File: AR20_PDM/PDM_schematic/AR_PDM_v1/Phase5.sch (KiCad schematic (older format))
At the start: 15 parts, among them Q1 BTS50025-1TAD, U1 INA233

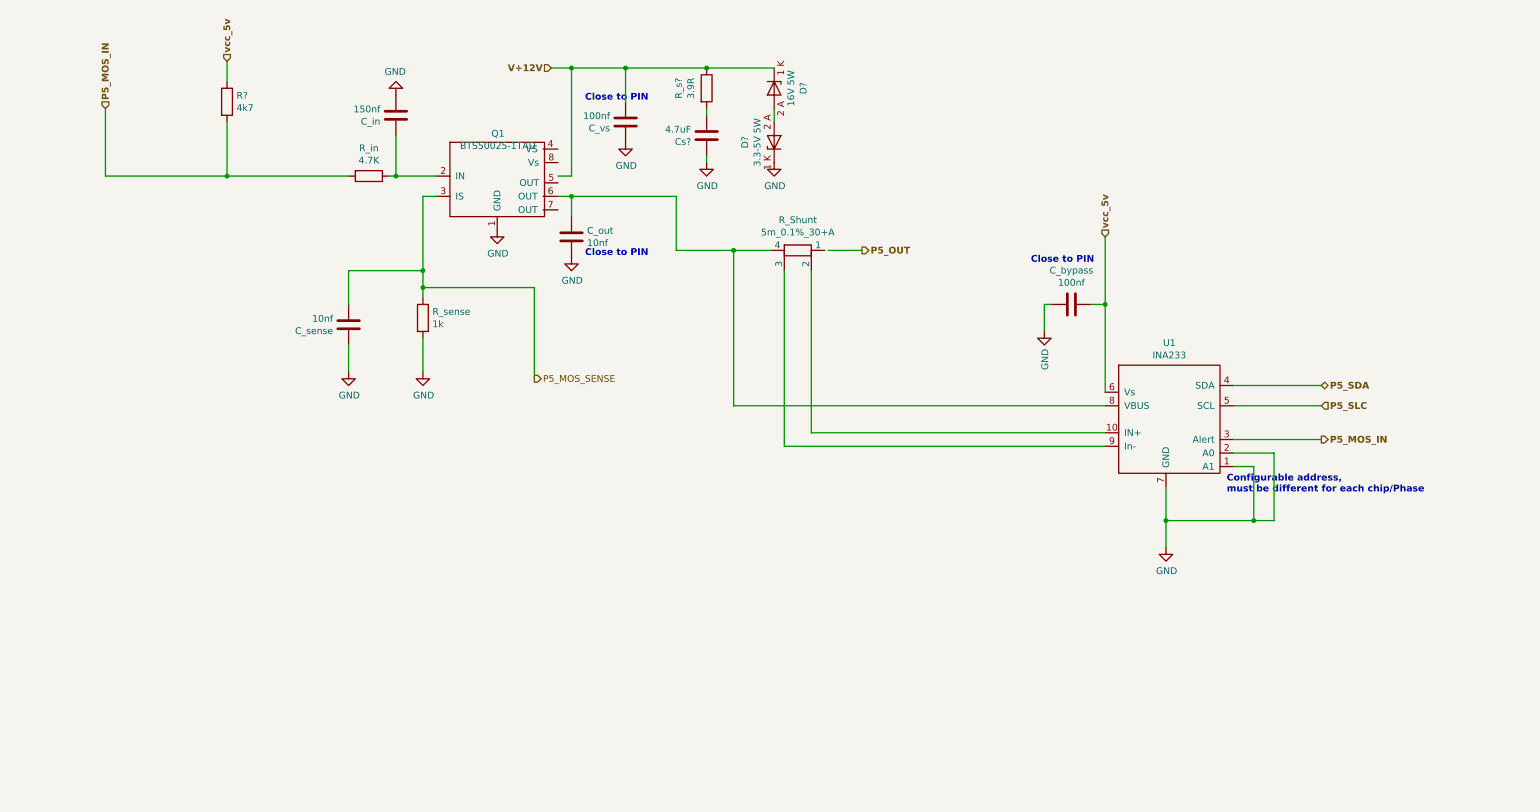
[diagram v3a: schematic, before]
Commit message: Fixed issues, controlled components, BOM, see discription
- added acm symbol
- fixed wrongly faced P-mosfets
- I/O expander now sinks led instead of source
- Bill of material mostly done
- Correct address for INA233 chips.
- Now 4 diodes serves as flyback for all mosfets
- Corrected naming scheme for compmonents (everything is not fixed yet)
- Fixed some labels
- altso some minor changes
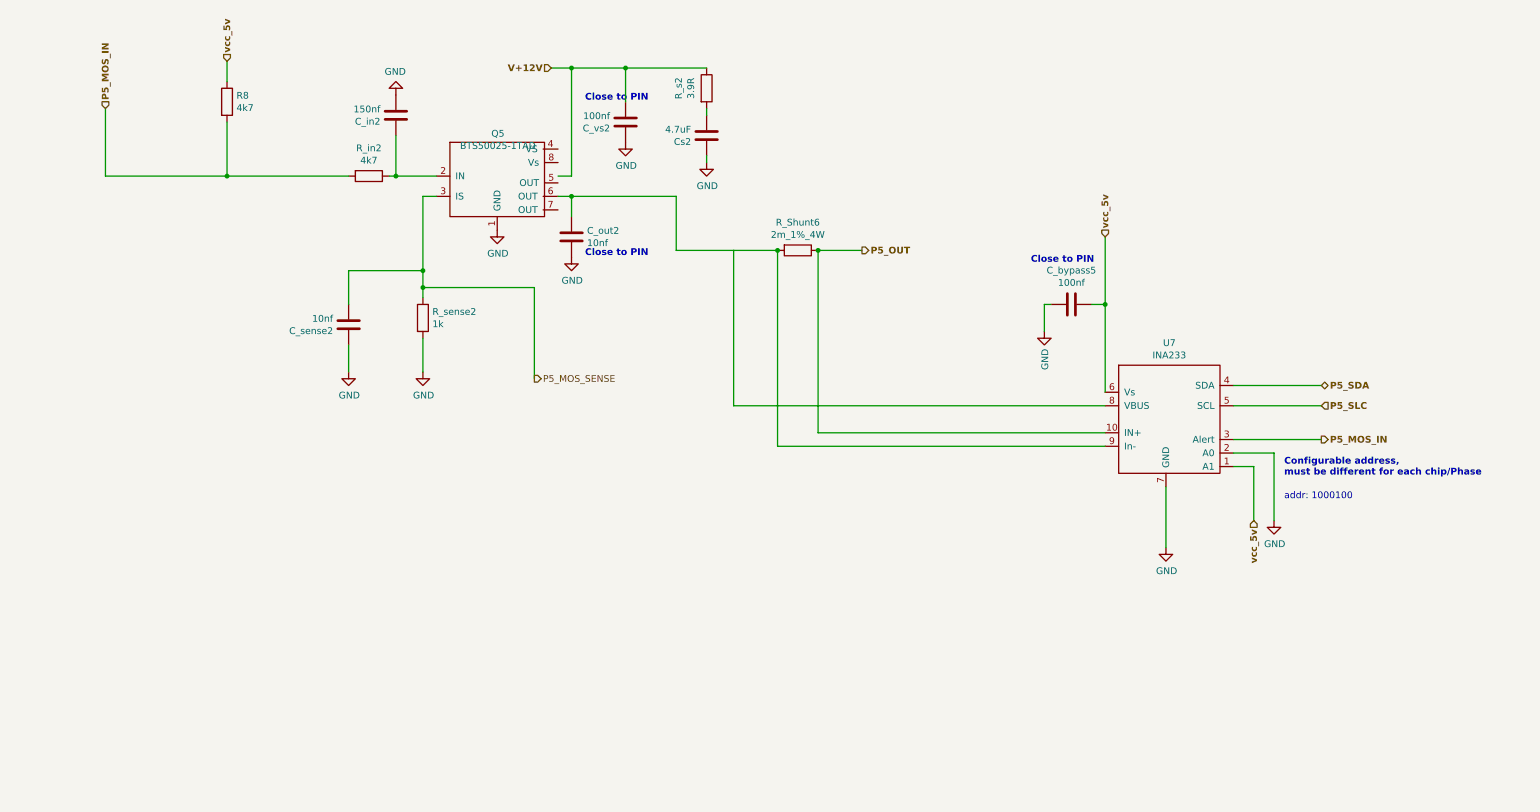
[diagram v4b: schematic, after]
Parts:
- removed C_bypass: 100nf, symbol AR20_PDM_v1-rescue:C-Device
- removed C_in: 150nf, symbol AR20_PDM_v1-rescue:C-Device
- removed C_out, C_sense: 10nf, symbol AR20_PDM_v1-rescue:C-Device
- removed Cs?: 4.7uF, symbol AR20_PDM_v1-rescue:C-Device
- removed D?: 3.3-5V 5W, symbol AR20_PDM_v1-rescue:D_Zener-Device
- removed D?: 16V 5W, symbol AR20_PDM_v1-rescue:D_Zener-Device
- removed Q1: BTS50025-1TAD, symbol AR20_PDM_v1-rescue:BTS50025-1TAD
- removed R?: 4k7, symbol AR20_PDM_v1-rescue:R-Device
- removed R_Shunt: 5m_0.1%_30+A, symbol AR20_PDM_v1-rescue:R_Shunt-Device
- removed R_in: 4.7K, symbol AR20_PDM_v1-rescue:R-Device
- removed R_s?: 3.9R, symbol AR20_PDM_v1-rescue:R-Device
- removed R_sense: 1k, symbol AR20_PDM_v1-rescue:R-Device
- removed U1: INA233, symbol AR20_PDM_v1-rescue:INA233
- added C_bypass5: 100nf, Capacitor_SMD:C_0603_1608Metric, symbol AR20_PDM_v1-rescue:C-Device
- added C_in2: 150nf, Capacitor_SMD:C_0603_1608Metric, symbol AR20_PDM_v1-rescue:C-Device
- added C_out2, C_sense2: 10nf, Capacitor_SMD:C_0603_1608Metric, symbol AR20_PDM_v1-rescue:C-Device
- added Cs2: 4.7uF, Capacitor_SMD:C_1206_3216Metric, symbol AR20_PDM_v1-rescue:C-Device
- added Q5: BTS50025-1TAD, symbol AR20_PDM_v1-rescue:BTS50025-1TAD
- added R8, R_in2: 4k7, symbol AR20_PDM_v1-rescue:R-Device
- added R_Shunt6: 2m_1%_4W, symbol AR20_PDM_v1-rescue:R-Device
- added R_s2: 3.9R, symbol AR20_PDM_v1-rescue:R-Device
- added R_sense2: 1k, symbol AR20_PDM_v1-rescue:R-Device
- added U7: INA233, symbol AR20_PDM_v1-rescue:INA233
- C_vs2: renamed from C_vs; footprint (none) -> Capacitor_SMD:C_0603_1608Metric
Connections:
- wire segments 57 -> 52
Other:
- note added: "addr: 1000100"

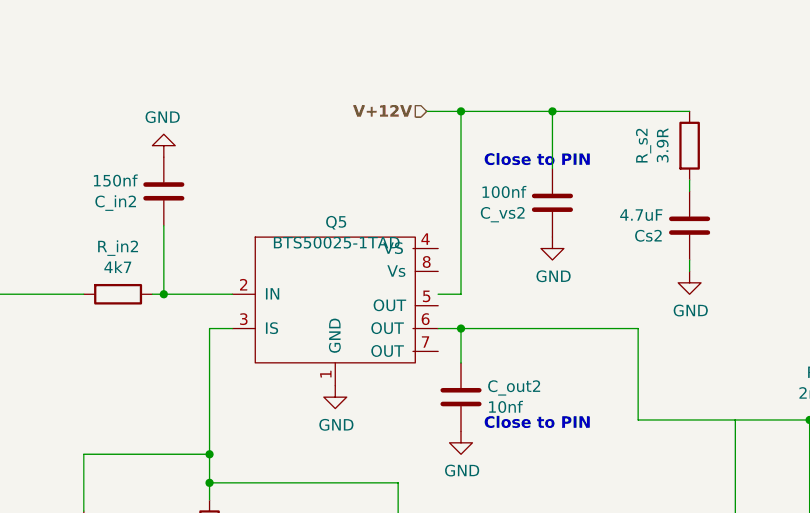
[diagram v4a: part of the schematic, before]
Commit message: PCB design, and issue fixing, work in progress
- Error fixed: Mux mosfet resistor change to ground
- Open drain output added on phase 6, for engine blipping purpose
- Most of pcb symbols and footprints are finished, including main connector
- PCB is change from 1oz to 2oz copper layer, for easier routing.
- Basic Draft of pcb is done, for now.
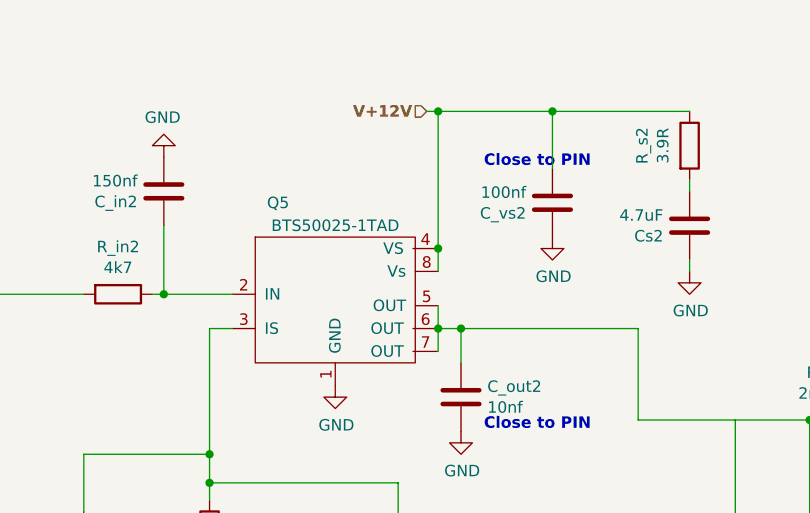
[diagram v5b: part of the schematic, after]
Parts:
- Q5: footprint (none) -> AR_PDM_v1:BTS500xx
- R8, R_in2, R_s2, R_sense2: footprint (none) -> Resistor_SMD:R_0603_1608Metric
- R_Shunt6: footprint (none) -> Resistor_SMD:R_2512_6332Metric
- U7: footprint (none) -> AR_PDM_v1:INA233
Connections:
- net V+12V: now also Q5.4 (VS), Q5.8 (Vs)
- net at C_out2.1, Q5.6 (OUT), R_Shunt6.2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: now also Q5.5 (OUT), Q5.7 (OUT)
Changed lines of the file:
@@
 F 0 "R_in2" V 3093 2400 50  0000 C CNN
 F 1 "4k7" V 3184 2400 50  0000 C CNN
-F 2 "" V 3230 2400 50  0001 C CNN
+F 2 "Resistor_SMD:R_0603_1608Metric" V 3230 2400 50  0001 C CNN
 F 3 "~" H 3300 2400 50  0001 C CNN
 	1    3300 2400
@@
 F 0 "R8" H 2320 1896 50  0000 L CNN
 F 1 "4k7" H 2320 1805 50  0000 L CNN
-F 2 "" V 2180 1850 50  0001 C CNN
+F 2 "Resistor_SMD:R_0603_1608Metric" V 2180 1850 50  0001 C CNN
 F 3 "~" H 2250 1850 50  0001 C CNN
 	1    2250 1850
@@
 AR Path="/5E0FDCCC/5E21B7FF" Ref="Q?"  Part="1"
 AR Path="/5E10174B/5E21B7FF" Ref="Q?"  Part="1"
-F 0 "Q5" H 4255 3215 50  0000 C CNN
-F 1 "BTS50025-1TAD" H 4255 3124 50  0000 C CNN
-F 2 "" H 4250 2650 50  0001 C CNN
+F 0 "Q5" H 4000 3300 50  0000 C CNN
+F 1 "BTS50025-1TAD" H 4250 3200 50  0000 C CNN
+F 2 "AR_PDM_v1:BTS500xx" H 4250 2650 50  0001 C CNN
 F 3 "" H 4250 2650 50  0001 C CNN
 	1    4250 2650
@@
 F 0 "U7" H 9225 4465 50  0000 C CNN
 F 1 "INA233" H 9225 4374 50  0000 C CNN
-F 2 "" H 9200 4050 50  0001 C CNN
+F 2 "AR_PDM_v1:INA233" H 9200 4050 50  0001 C CNN
 F 3 "" H 9200 4050 50  0001 C CNN
 	1    9200 4050
@@
 Wire Wire Line
 	3700 3100 3700 3225
-Wire Wire Line
-	4700 2400 4800 2400
-Wire Wire Line
-	4800 2400 4800 1600
-Wire Wire Line
-	4800 1600 4650 1600
 Text HLabel 2250 1550 1    50   Input ~ 10
 vcc_5v
@@
 F 0 "R_s2" V 5593 1750 50  0000 C CNN
 F 1 "3.9R" V 5684 1750 50  0000 C CNN
-F 2 "" V 5730 1750 50  0001 C CNN
+F 2 "Resistor_SMD:R_0603_1608Metric" V 5730 1750 50  0001 C CNN
 F 3 "~" H 5800 1750 50  0001 C CNN
 	1    5800 1750
@@
 Wire Wire Line
 	5200 1600 5800 1600
-Wire Wire Line
-	4800 1600 5200 1600
-Connection ~ 4800 1600
 Connection ~ 5200 1600
 Text HLabel 1350 1900 1    50   Input ~ 10
@@
 F 0 "R_sense2" H 3770 3496 50  0000 L CNN
 F 1 "1k" H 3770 3405 50  0000 L CNN
-F 2 "" V 3630 3450 50  0001 C CNN
+F 2 "Resistor_SMD:R_0603_1608Metric" V 3630 3450 50  0001 C CNN
 F 3 "~" H 3700 3450 50  0001 C CNN
 	1    3700 3450
@@
 F 0 "R_Shunt6" V 6268 2950 50  0000 C CNN
 F 1 "2m_1%_4W" V 6359 2950 50  0000 C CNN
-F 2 "" V 6405 2950 50  0001 C CNN
+F 2 "Resistor_SMD:R_2512_6332Metric" V 6405 2950 50  0001 C CNN
 F 3 "~" H 6475 2950 50  0001 C CNN
 	1    6475 2950
@@
 Text HLabel 9850 4950 3    50   Input ~ 10
 vcc_5v
+Wire Wire Line
+	4700 2550 4700 2650
+Connection ~ 4700 2550
+Wire Wire Line
+	4700 2550 4700 2450
+Wire Wire Line
+	4650 1600 4700 1600
+Wire Wire Line
+	4700 2300 4700 2200
+Wire Wire Line
+	4700 2200 4700 1600
+Connection ~ 4700 2200
+Connection ~ 4700 1600
+Wire Wire Line
+	4700 1600 5200 1600
 $EndSCHEMATC

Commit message: PCB Design, Work in progress
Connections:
- net P5_Shunt: now reaches C_out2.1, Q5.5 (OUT), Q5.6 (OUT), Q5.7 (OUT), R_Shunt6.2, U7.8 (VBUS), U7.9 (In-)
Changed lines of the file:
@@
 $Descr A4 11693 8268
 encoding utf-8
-Sheet 6 13
+Sheet 5 13
 Title ""
 Date ""
@@
 Wire Wire Line
 	4700 1600 5200 1600
+Wire Wire Line
+	6000 2950 6000 2825
+Text HLabel 6000 2825 1    50   Input ~ 0
+P5_Shunt
+Connection ~ 6000 2950
 $EndSCHEMATC

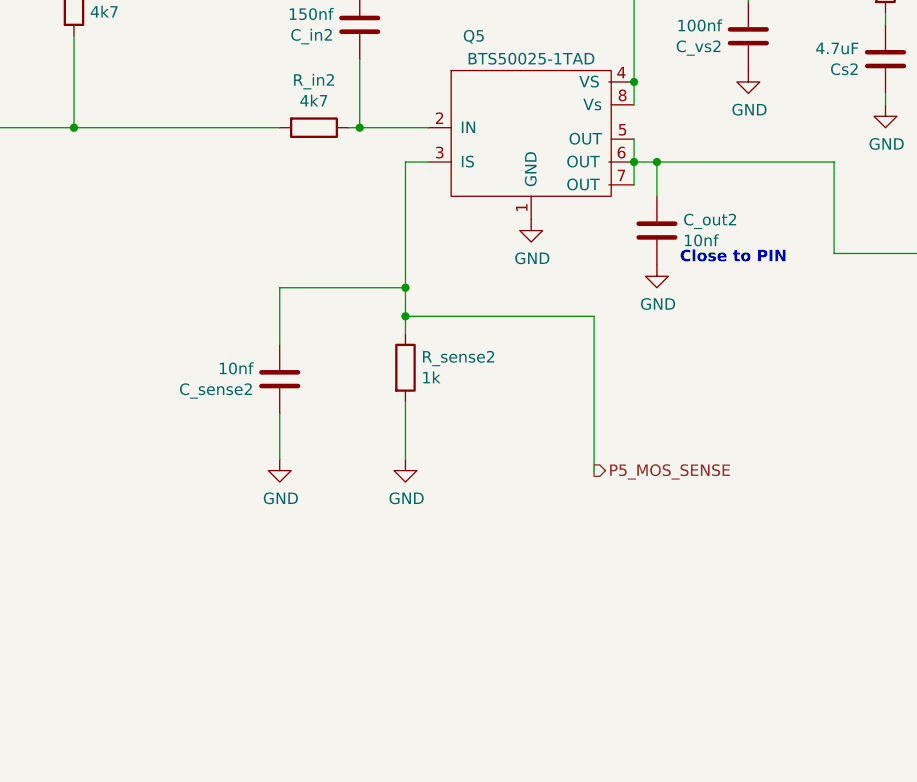
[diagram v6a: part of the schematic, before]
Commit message: PCB Design,  minor schematics changes, work in progress, see description
- Removed mos sense caps and resistors accept one, 
since only one measurement can be done, at a time.
- added mos sens protection resistors on each line, to protect mux mosfets and micro controller. 
- Routing plan mostly finalized, some of the traces are just proof of concept.
those needs to be routed nicely.
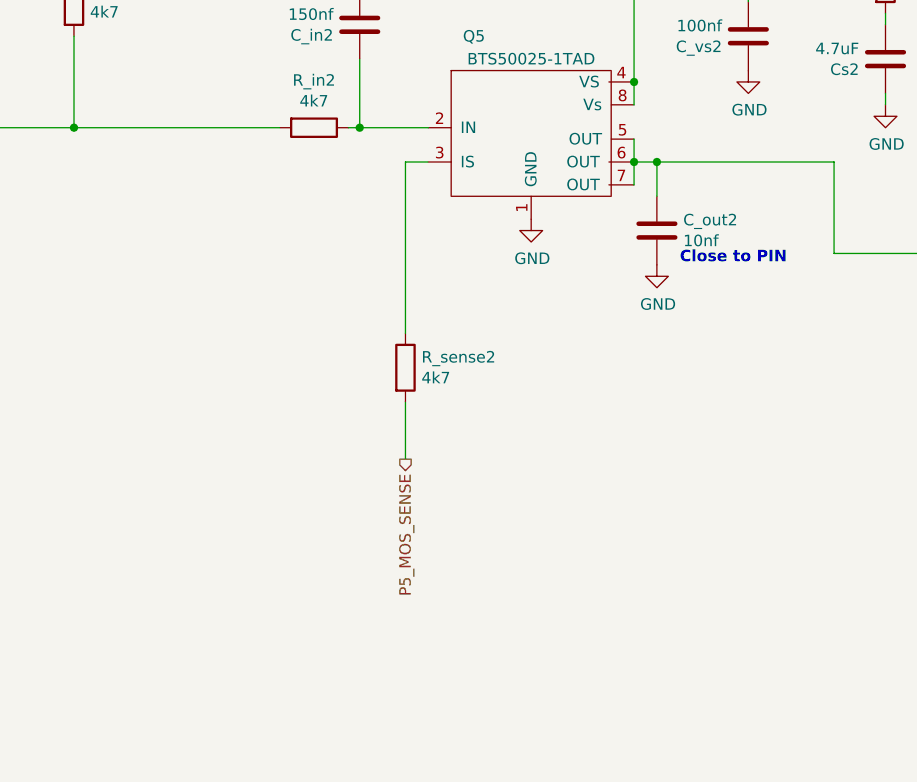
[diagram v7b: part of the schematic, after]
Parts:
- removed C_sense2: 10nf, Capacitor_SMD:C_0603_1608Metric, symbol AR20_PDM_v1-rescue:C-Device
- R_sense2: value 1k -> 4k7
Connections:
- net GND: no longer R_sense2.2
- net P5_MOS_SENSE: now also R_sense2.2; no longer Q5.3 (IS), R_sense2.1
- new net: Q5.3 (IS), R_sense2.1
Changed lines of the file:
@@
-$EndComp
-$Comp
-L AR20_PDM_v1-rescue:GND-power #PWR?
-U 1 1 5E21B821
-P 3700 3850
-AR Path="/5DA89415/5E21B821" Ref="#PWR?"  Part="1"
-AR Path="/5DEB10A1/5E21B821" Ref="#PWR?"  Part="1"
-AR Path="/5DEB20EA/5E21B821" Ref="#PWR?"  Part="1"
-AR Path="/5E0E4725/5E21B821" Ref="#PWR?"  Part="1"
-AR Path="/5E0E4A93/5E21B821" Ref="#PWR?"  Part="1"
-AR Path="/5E0E4EB5/5E21B821" Ref="#PWR?"  Part="1"
-AR Path="/5E0E5304/5E21B821" Ref="#PWR?"  Part="1"
-AR Path="/5E0E594B/5E21B821" Ref="#PWR?"  Part="1"
-AR Path="/5E0E607C/5E21B821" Ref="#PWR?"  Part="1"
-AR Path="/5E0FB5C8/5E21B821" Ref="#PWR?"  Part="1"
-AR Path="/5E0FBBBD/5E21B821" Ref="#PWR?"  Part="1"
-AR Path="/5E0FC3A2/5E21B821" Ref="#PWR?"  Part="1"
-AR Path="/5E0FCFDC/5E21B821" Ref="#PWR046"  Part="1"
-AR Path="/5E0FDCCC/5E21B821" Ref="#PWR?"  Part="1"
-AR Path="/5E10174B/5E21B821" Ref="#PWR?"  Part="1"
-F 0 "#PWR046" H 3700 3600 50  0001 C CNN
-F 1 "GND" H 3705 3677 50  0000 C CNN
-F 2 "" H 3700 3850 50  0001 C CNN
-F 3 "" H 3700 3850 50  0001 C CNN
-	1    3700 3850
-	1    0    0    -1
 $EndComp
 $Comp
@@
 $EndComp
 Wire Wire Line
-	3700 2550 3700 3100
-Wire Wire Line
 	3700 2550 3800 2550
 Wire Wire Line
@@
 Wire Wire Line
 	9700 4450 10000 4450
-$Comp
-L AR20_PDM_v1-rescue:GND-power #PWR?
-U 1 1 5E21B849
-P 3150 3850
-AR Path="/5DA89415/5E21B849" Ref="#PWR?"  Part="1"
-AR Path="/5DEB10A1/5E21B849" Ref="#PWR?"  Part="1"
-AR Path="/5DEB20EA/5E21B849" Ref="#PWR?"  Part="1"
-AR Path="/5E0E4725/5E21B849" Ref="#PWR?"  Part="1"
-AR Path="/5E0E4A93/5E21B849" Ref="#PWR?"  Part="1"
-AR Path="/5E0E4EB5/5E21B849" Ref="#PWR?"  Part="1"
-AR Path="/5E0E5304/5E21B849" Ref="#PWR?"  Part="1"
-AR Path="/5E0E594B/5E21B849" Ref="#PWR?"  Part="1"
-AR Path="/5E0E607C/5E21B849" Ref="#PWR?"  Part="1"
-AR Path="/5E0FB5C8/5E21B849" Ref="#PWR?"  Part="1"
-AR Path="/5E0FBBBD/5E21B849" Ref="#PWR?"  Part="1"
-AR Path="/5E0FC3A2/5E21B849" Ref="#PWR?"  Part="1"
-AR Path="/5E0FCFDC/5E21B849" Ref="#PWR044"  Part="1"
-AR Path="/5E0FDCCC/5E21B849" Ref="#PWR?"  Part="1"
-AR Path="/5E10174B/5E21B849" Ref="#PWR?"  Part="1"
-F 0 "#PWR044" H 3150 3600 50  0001 C CNN
-F 1 "GND" H 3155 3677 50  0000 C CNN
-F 2 "" H 3150 3850 50  0001 C CNN
-F 3 "" H 3150 3850 50  0001 C CNN
-	1    3150 3850
-	1    0    0    -1
-$EndComp
-$Comp
-L AR20_PDM_v1-rescue:C-Device C_sense?
-U 1 1 5E21B850
-P 3150 3500
-AR Path="/5DA89415/5E21B850" Ref="C_sense?"  Part="1"
-AR Path="/5DEB10A1/5E21B850" Ref="C_sense?"  Part="1"
-AR Path="/5DEB20EA/5E21B850" Ref="C_sense?"  Part="1"
-AR Path="/5E0E4725/5E21B850" Ref="C_sense?"  Part="1"
-AR Path="/5E0E4A93/5E21B850" Ref="C_sense?"  Part="1"
-AR Path="/5E0E4EB5/5E21B850" Ref="C_sense?"  Part="1"
-AR Path="/5E0E5304/5E21B850" Ref="C_sense?"  Part="1"
-AR Path="/5E0E594B/5E21B850" Ref="C_sense?"  Part="1"
-AR Path="/5E0E607C/5E21B850" Ref="C_sense?"  Part="1"
-AR Path="/5E0FB5C8/5E21B850" Ref="C_sense?"  Part="1"
-AR Path="/5E0FBBBD/5E21B850" Ref="C_sense?"  Part="1"
-AR Path="/5E0FC3A2/5E21B850" Ref="C_sense?"  Part="1"
-AR Path="/5E0FCFDC/5E21B850" Ref="C_sense2"  Part="1"
-AR Path="/5E0FDCCC/5E21B850" Ref="C_sense?"  Part="1"
-AR Path="/5E10174B/5E21B850" Ref="C_sense?"  Part="1"
-F 0 "C_sense2" H 3265 3546 50  0000 L CNN
-F 1 "10nf" H 3265 3455 50  0000 L CNN
-F 2 "Capacitor_SMD:C_0603_1608Metric" H 3188 3350 50  0001 C CNN
-F 3 "~" H 3150 3500 50  0001 C CNN
-	1    3150 3500
-	-1   0    0    1
-$EndComp
 Wire Wire Line
 	3450 2400 3500 2400
@@
 Text Notes 8200 3050 0    50   ~ 10
 Close to PIN
-Wire Wire Line
-	3150 3100 3150 3350
-Wire Wire Line
-	3150 3650 3150 3850
-Wire Wire Line
-	3150 3100 3700 3100
-Connection ~ 3700 3100
-Wire Wire Line
-	3700 3100 3700 3225
 Text HLabel 2250 1550 1    50   Input ~ 10
 vcc_5v
@@
 AR Path="/5E10174B/5E21B874" Ref="R_sense?"  Part="1"
 F 0 "R_sense2" H 3770 3496 50  0000 L CNN
-F 1 "1k" H 3770 3405 50  0000 L CNN
+F 1 "4k7" H 3770 3405 50  0000 L CNN
 F 2 "Resistor_SMD:R_0603_1608Metric" V 3630 3450 50  0001 C CNN
 F 3 "~" H 3700 3450 50  0001 C CNN
@@
 Wire Wire Line
 	6625 4300 8750 4300
-Wire Wire Line
-	3700 3225 4525 3225
-Wire Wire Line
-	4525 3225 4525 3900
-Connection ~ 3700 3225
-Wire Wire Line
-	3700 3225 3700 3300
-Text HLabel 4525 3900 2    50   Output ~ 0
+Text HLabel 3700 3850 3    50   Output ~ 0
 P5_MOS_SENSE
 Wire Wire Line
@@
 P5_Shunt
 Connection ~ 6000 2950
+Wire Wire Line
+	3700 2550 3700 3300
 $EndSCHEMATC
